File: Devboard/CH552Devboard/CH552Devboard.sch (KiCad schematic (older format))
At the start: 15 parts, among them J1 D+, J2 USB_B_Micro, J3 System, J4 0001, J5 0010, SW1 SW_Push, SW2 SW_Push, SW3 SW_Push, SW4 SW_Push, U1 CH552T

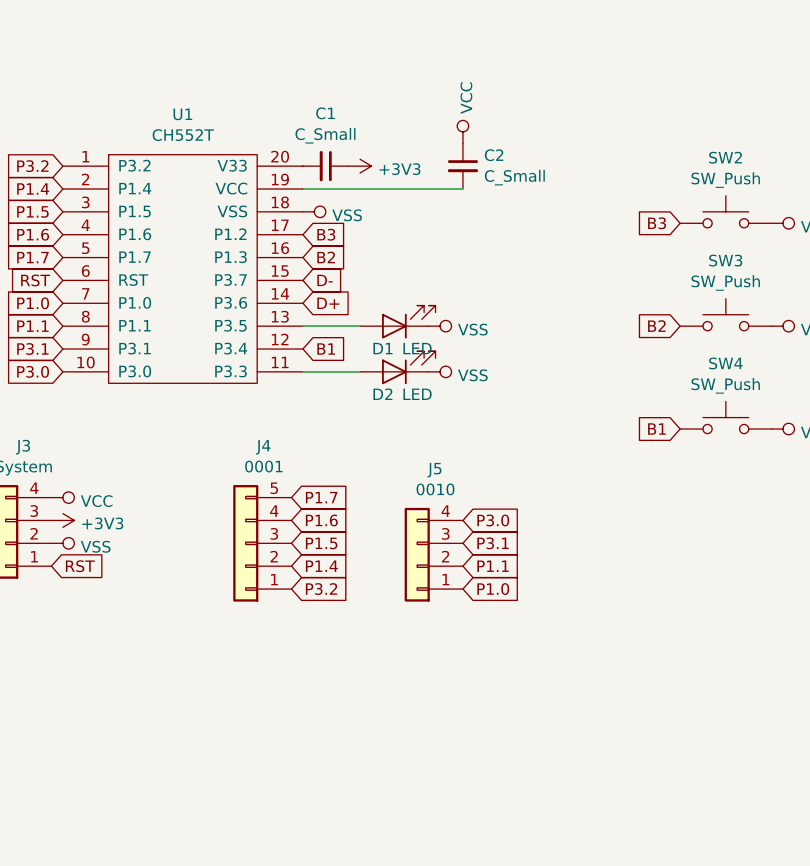
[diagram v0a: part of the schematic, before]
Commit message: Recieved V1, fixed issue. Seems to work now.
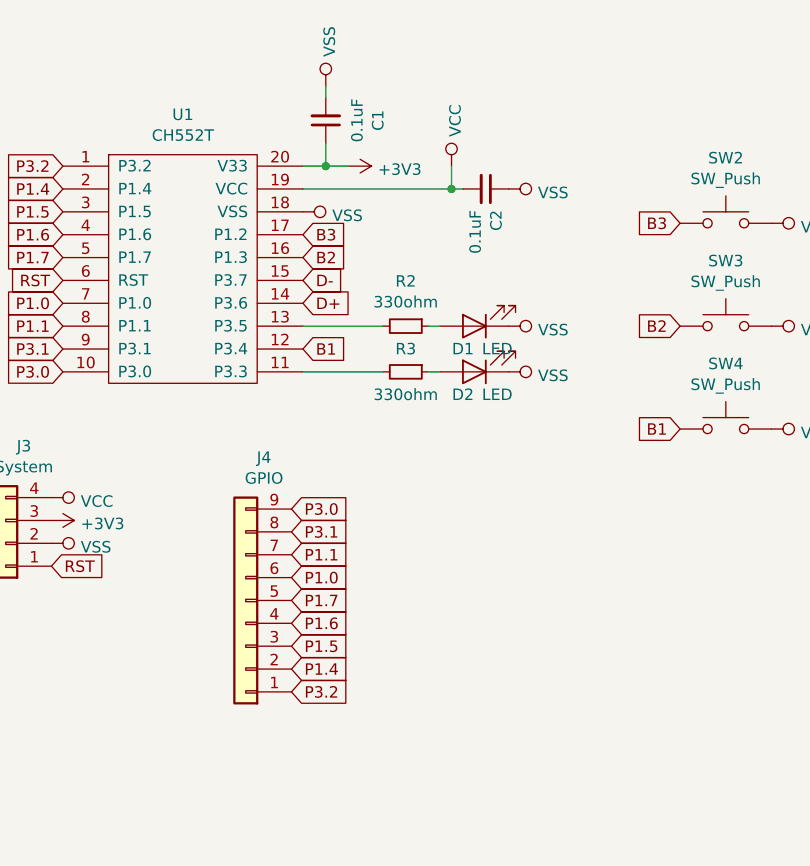
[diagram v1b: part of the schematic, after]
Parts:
- removed J4: 0001, Pin_Headers:Pin_Header_Straight_1x05_Pitch2.54mm, symbol Connector_Generic:Conn_01x05
- removed J5: 0010, Pin_Headers:Pin_Header_Straight_1x04_Pitch2.54mm, symbol Connector_Generic:Conn_01x04
- added J4: GPIO, Pin_Headers:Pin_Header_Straight_1x09_Pitch2.54mm, symbol Connector_Generic:Conn_01x09
- added R2, R3: 330ohm, Resistors_SMD:R_0805, symbol Device:R_Small
- C1, C2: value C_Small -> 0.1uF
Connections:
- net +3V3: now also U1.20 (V33)
- net P1.0: now also J4.6 (Pin_6)
- net P1.1: now also J4.7 (Pin_7)
- net P1.4: now also J4.2 (Pin_2)
- net P1.5: now also J4.3 (Pin_3)
- net P1.6: now also J4.4 (Pin_4)
- net P1.7: now also J4.5 (Pin_5)
- net P3.0: now also J4.9 (Pin_9)
- net P3.1: now also J4.8 (Pin_8)
- net P3.2: now also J4.1 (Pin_1)
- net VCC: now also C2.2, U1.19 (VCC); no longer C2.1
- net VSS: now also C1.2, C2.1
- net at U1.11 (P3.3): now also R3.2; no longer D2.2 (A)
- net at U1.13 (P3.5): now also R2.2; no longer D1.2 (A)
- new net: D1.2 (A), R2.1
- new net: D2.2 (A), R3.1
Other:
- moved on the sheet: C1, C2, D1, D2
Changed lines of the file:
@@
 EESchema Schematic File Version 4
+LIBS:CH552Devboard-cache
 EELAYER 26 0
 EELAYER END
@@
 L power:VCC #PWR08
 U 1 1 5C6D8649
-P 7550 3000
-F 0 "#PWR08" H 7550 2850 50  0001 C CNN
-F 1 "VCC" V 7567 3128 50  0000 L CNN
-F 2 "" H 7550 3000 50  0001 C CNN
-F 3 "" H 7550 3000 50  0001 C CNN
-	1    7550 3000
+P 7500 3100
+F 0 "#PWR08" H 7500 2950 50  0001 C CNN
+F 1 "VCC" V 7517 3228 50  0000 L CNN
+F 2 "" H 7500 3100 50  0001 C CNN
+F 3 "" H 7500 3100 50  0001 C CNN
+	1    7500 3100
 	1    0    0    -1
 $EndComp
@@
 Text GLabel 5750 4850 2    50   Input ~ 0
 RST
-$Comp
-L Connector_Generic:Conn_01x05 J4
-U 1 1 5C6D8F10
-P 6600 4750
-F 0 "J4" H 6520 4325 50  0000 C CNN
-F 1 "0001" H 6520 4416 50  0000 C CNN
-F 2 "Pin_Headers:Pin_Header_Straight_1x05_Pitch2.54mm" H 6600 4750 50  0001 C CNN
-F 3 "~" H 6600 4750 50  0001 C CNN
-	1    6600 4750
-	-1   0    0    1
-$EndComp
 Text GLabel 5800 3100 0    50   Input ~ 0
 P3.2
@@
 Text GLabel 5800 3500 0    50   Input ~ 0
 P1.7
-Text GLabel 6800 4950 2    50   Input ~ 0
+Text GLabel 6800 5400 2    50   Input ~ 0
 P3.2
-Text GLabel 6800 4850 2    50   Input ~ 0
+Text GLabel 6800 5300 2    50   Input ~ 0
 P1.4
-Text GLabel 6800 4750 2    50   Input ~ 0
+Text GLabel 6800 5200 2    50   Input ~ 0
 P1.5
-Text GLabel 6800 4650 2    50   Input ~ 0
+Text GLabel 6800 5100 2    50   Input ~ 0
 P1.6
-Text GLabel 6800 4550 2    50   Input ~ 0
+Text GLabel 6800 5000 2    50   Input ~ 0
 P1.7
-$Comp
-L Connector_Generic:Conn_01x04 J5
-U 1 1 5C6D9089
-P 7350 4850
-F 0 "J5" H 7270 4425 50  0000 C CNN
-F 1 "0010" H 7270 4516 50  0000 C CNN
-F 2 "Pin_Headers:Pin_Header_Straight_1x04_Pitch2.54mm" H 7350 4850 50  0001 C CNN
-F 3 "~" H 7350 4850 50  0001 C CNN
-	1    7350 4850
-	-1   0    0    1
-$EndComp
 Text GLabel 5800 3700 0    50   Input ~ 0
 P1.0
@@
 Text GLabel 5800 4000 0    50   Input ~ 0
 P3.0
-Text GLabel 7550 4950 2    50   Input ~ 0
+Text GLabel 6800 4900 2    50   Input ~ 0
 P1.0
-Text GLabel 7550 4850 2    50   Input ~ 0
+Text GLabel 6800 4800 2    50   Input ~ 0
 P1.1
-Text GLabel 7550 4750 2    50   Input ~ 0
+Text GLabel 6800 4700 2    50   Input ~ 0
 P3.1
-Text GLabel 7550 4650 2    50   Input ~ 0
+Text GLabel 6800 4600 2    50   Input ~ 0
 P3.0
 Text GLabel 5800 3600 0    50   Input ~ 0
@@
 L Device:LED D1
 U 1 1 5C6D95BF
-P 7250 3800
-F 0 "D1" H 7300 3900 50  0000 C CNN
-F 1 "LED" H 7150 3900 50  0000 C CNN
-F 2 "LEDs:LED_0805" H 7250 3800 50  0001 C CNN
-F 3 "~" H 7250 3800 50  0001 C CNN
-	1    7250 3800
+P 7600 3800
+F 0 "D1" H 7650 3900 50  0000 C CNN
+F 1 "LED" H 7500 3900 50  0000 C CNN
+F 2 "LEDs:LED_0805" H 7600 3800 50  0001 C CNN
+F 3 "~" H 7600 3800 50  0001 C CNN
+	1    7600 3800
 	-1   0    0    1
 $EndComp
@@
 L Device:LED D2
 U 1 1 5C6D961E
-P 7250 4000
-F 0 "D2" H 7300 4100 50  0000 C CNN
-F 1 "LED" H 7150 4100 50  0000 C CNN
-F 2 "LEDs:LED_0805" H 7250 4000 50  0001 C CNN
-F 3 "~" H 7250 4000 50  0001 C CNN
-	1    7250 4000
+P 7600 4000
+F 0 "D2" H 7650 4100 50  0000 C CNN
+F 1 "LED" H 7500 4100 50  0000 C CNN
+F 2 "LEDs:LED_0805" H 7600 4000 50  0001 C CNN
+F 3 "~" H 7600 4000 50  0001 C CNN
+	1    7600 4000
 	-1   0    0    1
 $EndComp
@@
 L power:VSS #PWR010
 U 1 1 5C6D97AA
-P 7400 3800
-F 0 "#PWR010" H 7400 3650 50  0001 C CNN
-F 1 "VSS" V 7417 3928 50  0000 L CNN
-F 2 "" H 7400 3800 50  0001 C CNN
-F 3 "" H 7400 3800 50  0001 C CNN
-	1    7400 3800
+P 7750 3800
+F 0 "#PWR010" H 7750 3650 50  0001 C CNN
+F 1 "VSS" V 7767 3928 50  0000 L CNN
+F 2 "" H 7750 3800 50  0001 C CNN
+F 3 "" H 7750 3800 50  0001 C CNN
+	1    7750 3800
 	0    1    1    0
 $EndComp
@@
 L power:VSS #PWR011
 U 1 1 5C6D984F
-P 7400 4000
-F 0 "#PWR011" H 7400 3850 50  0001 C CNN
-F 1 "VSS" V 7417 4128 50  0000 L CNN
-F 2 "" H 7400 4000 50  0001 C CNN
-F 3 "" H 7400 4000 50  0001 C CNN
-	1    7400 4000
-	0    1    1    0
-$EndComp
-Wire Wire Line
-	6850 4000 7100 4000
-Wire Wire Line
-	6850 3800 7100 3800
+P 7750 4000
+F 0 "#PWR011" H 7750 3850 50  0001 C CNN
+F 1 "VSS" V 7767 4128 50  0000 L CNN
+F 2 "" H 7750 4000 50  0001 C CNN
+F 3 "" H 7750 4000 50  0001 C CNN
+	1    7750 4000
+	0    1    1    0
+$EndComp
 Text GLabel 6850 3900 2    50   Input ~ 0
 B1
@@
 L Device:C_Small C1
 U 1 1 5C6DB905
-P 6950 3100
-F 0 "C1" V 6721 3100 50  0000 C CNN
-F 1 "C_Small" V 6812 3100 50  0000 C CNN
-F 2 "Capacitors_SMD:C_0805" H 6950 3100 50  0001 C CNN
-F 3 "~" H 6950 3100 50  0001 C CNN
-	1    6950 3100
-	0    1    1    0
+P 6950 2900
+F 0 "C1" V 6721 2900 50  0000 C CNN
+F 1 "0.1uF" V 6812 2900 50  0000 C CNN
+F 2 "Capacitors_SMD:C_0805" H 6950 2900 50  0001 C CNN
+F 3 "~" H 6950 2900 50  0001 C CNN
+	1    6950 2900
+	-1   0    0    1
 $EndComp
 $Comp
 L Device:C_Small C2
 U 1 1 5C6DBA44
-P 7550 3100
-F 0 "C2" H 7642 3146 50  0000 L CNN
-F 1 "C_Small" H 7642 3055 50  0000 L CNN
-F 2 "Capacitors_SMD:C_0805" H 7550 3100 50  0001 C CNN
-F 3 "~" H 7550 3100 50  0001 C CNN
-	1    7550 3100
-	1    0    0    -1
-$EndComp
-Wire Wire Line
-	7550 3200 6850 3200
+P 7650 3200
+F 0 "C2" H 7742 3246 50  0000 L CNN
+F 1 "0.1uF" H 7742 3155 50  0000 L CNN
+F 2 "Capacitors_SMD:C_0805" H 7650 3200 50  0001 C CNN
+F 3 "~" H 7650 3200 50  0001 C CNN
+	1    7650 3200
+	0    1    1    0
+$EndComp
+Wire Wire Line
+	7550 3200 7500 3200
+$Comp
+L Connector_Generic:Conn_01x09 J4
+U 1 1 5C6DC28D
+P 6600 5000
+F 0 "J4" H 6520 4375 50  0000 C CNN
+F 1 "GPIO" H 6520 4466 50  0000 C CNN
+F 2 "Pin_Headers:Pin_Header_Straight_1x09_Pitch2.54mm" H 6600 5000 50  0001 C CNN
+F 3 "~" H 6600 5000 50  0001 C CNN
+	1    6600 5000
+	-1   0    0    1
+$EndComp
+Wire Wire Line
+	7500 3100 7500 3200
+Connection ~ 7500 3200
+Wire Wire Line
+	7500 3200 6850 3200
+Wire Wire Line
+	6850 3100 6950 3100
+Wire Wire Line
+	6950 3000 6950 3100
+Connection ~ 6950 3100
+Wire Wire Line
+	6950 3100 7050 3100
+Wire Wire Line
+	6950 2800 6950 2750
+$Comp
+L Device:R_Small R2
+U 1 1 5C7F48CB
+P 7300 3800
+F 0 "R2" V 7104 3800 50  0000 C CNN
+F 1 "330ohm" V 7195 3800 50  0000 C CNN
+F 2 "Resistors_SMD:R_0805" H 7300 3800 50  0001 C CNN
+F 3 "~" H 7300 3800 50  0001 C CNN
+	1    7300 3800
+	0    1    1    0
+$EndComp
+$Comp
+L Device:R_Small R3
+U 1 1 5C7F492B
+P 7300 4000
+F 0 "R3" V 7200 4000 50  0000 C CNN
+F 1 "330ohm" V 7400 4000 50  0000 C CNN
+F 2 "Resistors_SMD:R_0805" H 7300 4000 50  0001 C CNN
+F 3 "~" H 7300 4000 50  0001 C CNN
+	1    7300 4000
+	0    1    1    0
+$EndComp
+Wire Wire Line
+	7400 3800 7450 3800
+Wire Wire Line
+	7400 4000 7450 4000
+Wire Wire Line
+	6850 4000 7200 4000
+Wire Wire Line
+	6850 3800 7200 3800
+$Comp
+L power:VSS #PWR?
+U 1 1 5C7F52C2
+P 7750 3200
+F 0 "#PWR?" H 7750 3050 50  0001 C CNN
+F 1 "VSS" V 7767 3328 50  0000 L CNN
+F 2 "" H 7750 3200 50  0001 C CNN
+F 3 "" H 7750 3200 50  0001 C CNN
+	1    7750 3200
+	0    1    1    0
+$EndComp
+$Comp
+L power:VSS #PWR?
+U 1 1 5C7F52ED
+P 6950 2750
+F 0 "#PWR?" H 6950 2600 50  0001 C CNN
+F 1 "VSS" V 6967 2878 50  0000 L CNN
+F 2 "" H 6950 2750 50  0001 C CNN
+F 3 "" H 6950 2750 50  0001 C CNN
+	1    6950 2750
+	1    0    0    -1
+$EndComp
 $EndSCHEMATC

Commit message: Added silkscreen to devboard
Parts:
- U1: symbol CH552:CH552T -> CH552Devboard-rescue:CH552T-CH552
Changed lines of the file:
@@
 $EndDescr
 $Comp
-L CH552:CH552T U1
+L CH552Devboard-rescue:CH552T-CH552 U1
 U 1 1 5C6D8296
 P 6300 3450
